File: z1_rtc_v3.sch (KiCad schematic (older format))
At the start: 61 parts, among them J1 Conn_01x05, J10 Conn_01x02, J2 61200621621, J3 Conn_01x11, J4 Conn_01x11, J5 Conn_01x11, J6 Conn_01x11, J7 691137710002, J8 USB_B_Micro, J9 Conn_01x02, U1 LCMXO2-1200HC-4SG32C, U2 ATmega328PB-AU, U3 FT230XS, Y1 Crystal_Small

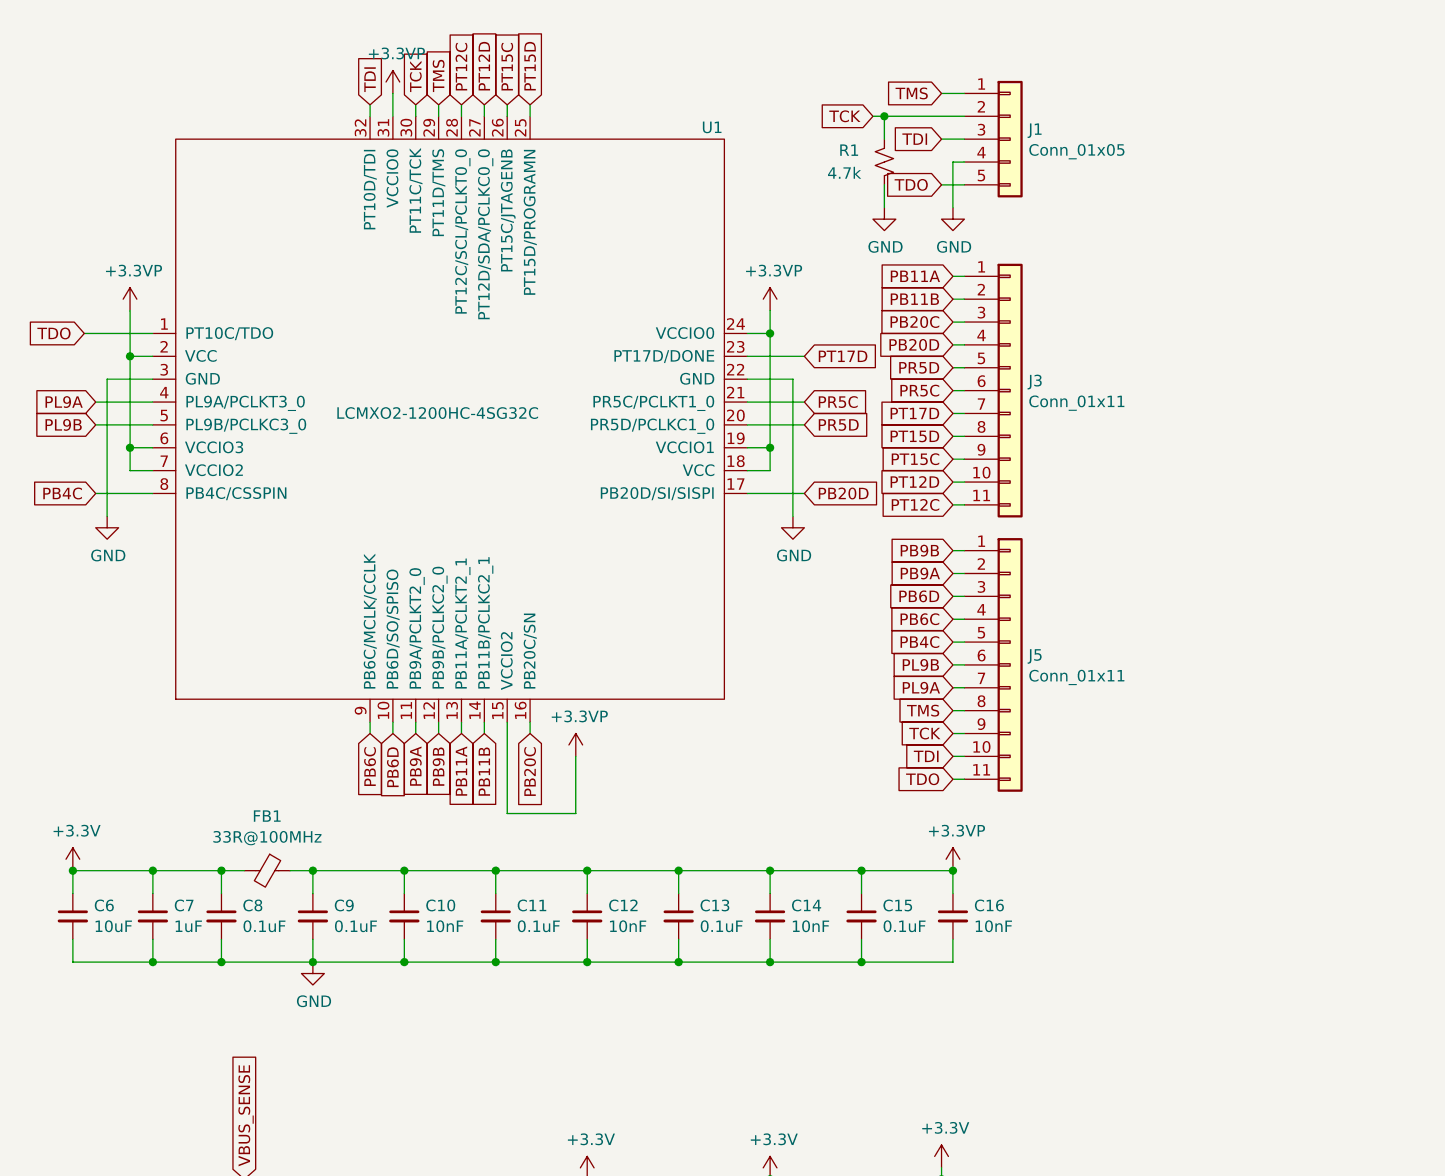
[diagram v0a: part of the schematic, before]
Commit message: board files for v3.2, with the tinyFPGA module
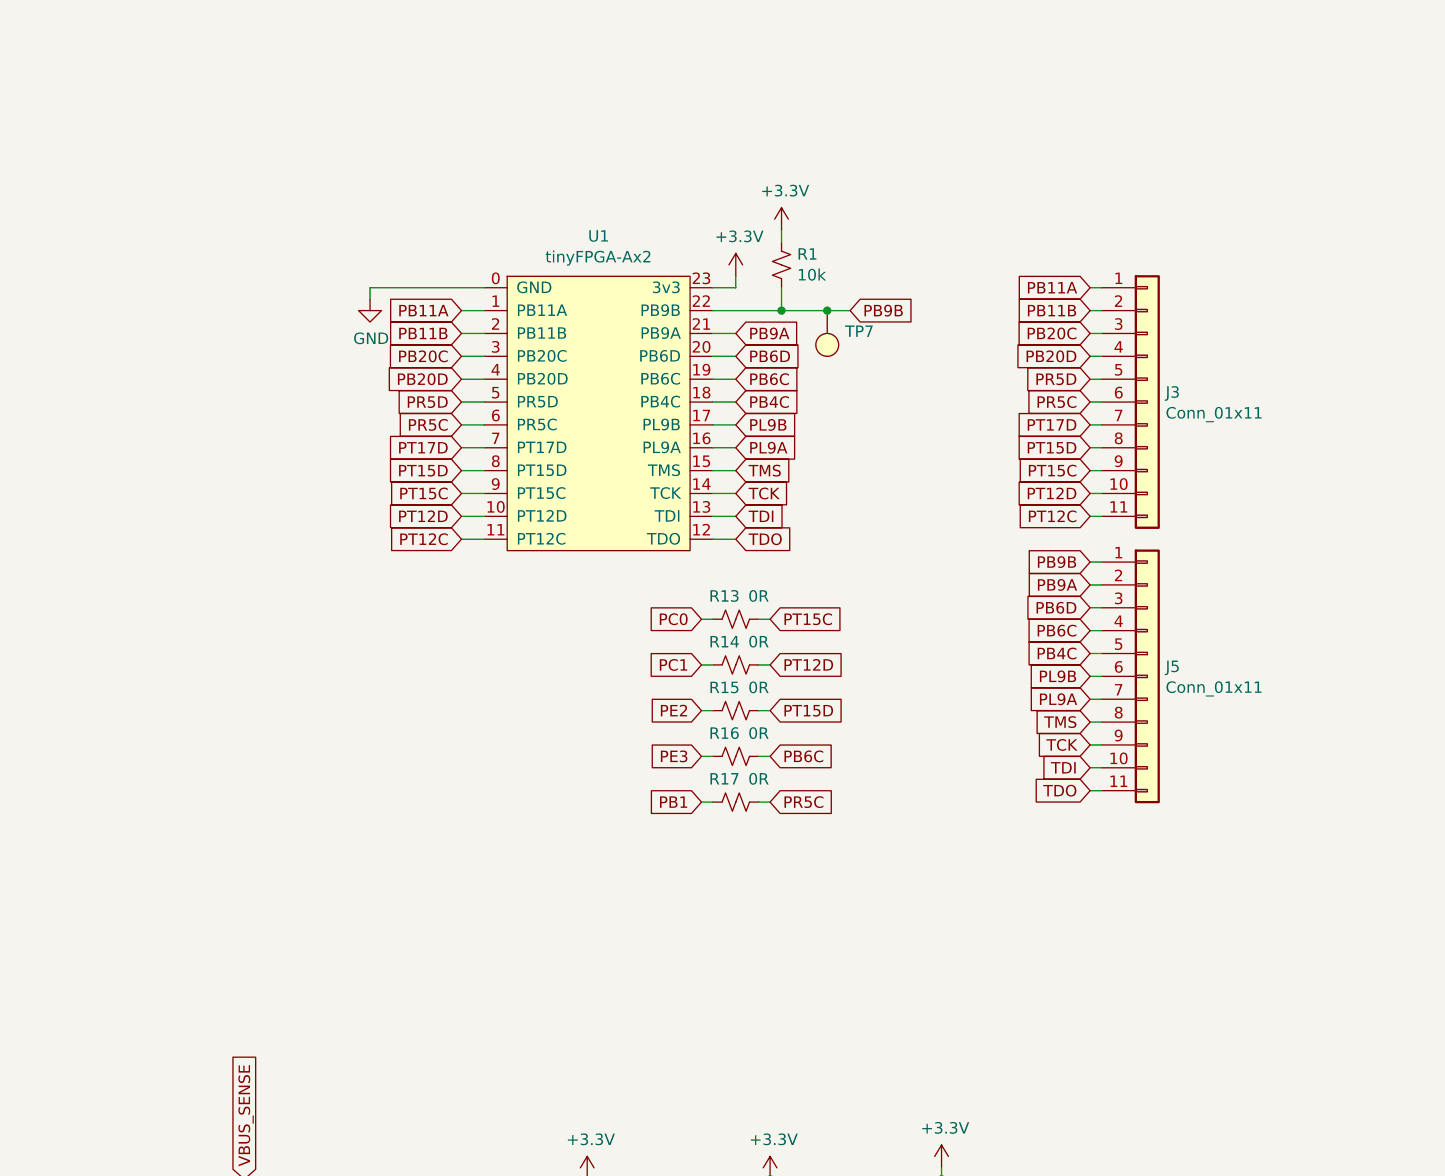
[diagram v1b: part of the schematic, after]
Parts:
- removed C10, C12, C14, C16: 10nF, Capacitor_SMD:C_0805_2012Metric, symbol Device:C_Small
- removed C11, C13, C15, C8, C9: 0.1uF, Capacitor_SMD:C_0603_1608Metric, symbol Device:C_Small
- removed C6: 10uF, Capacitor_SMD:C_0805_2012Metric, symbol Device:C_Small
- removed C7: 1uF, Capacitor_SMD:C_0603_1608Metric, symbol Device:C_Small
- removed FB1: 33R@100MHz, Capacitor_SMD:C_0603_1608Metric, symbol Device:Ferrite_Bead_Small
- removed J1: Conn_01x05, Connector_PinHeader_2.54mm:PinHeader_1x05_P2.54mm_Vertical, symbol Connector_Generic:Conn_01x05
- removed U1: LCMXO2-1200HC-4SG32C, Package_DFN_QFN:QFN-32-1EP_5x5mm_P0.5mm_EP3.1x3.1mm, symbol z1_rtc_v3:LCMXO2-1200HC-4SG32C
- added R13, R14, R15, R16, R17: 0R, Resistor_SMD:R_0603_1608Metric, symbol Device:R_Small_US
- added TP7: testpoint_smd_circ, z1_rtc_v3:test_point_smd_circ, symbol z1_rtc_v3:testpoint_smd_circ
- added U1: tinyFPGA-Ax2, z1_rtc_v3:tinyFPGA-Ax2, symbol z1_rtc_v3:tinyFPGA-Ax2
- R1: value 4.7k -> 10k; pn CRGH0603F4K7 -> RC0603JR-0710KL
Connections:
- net +3V3: now also R1.1, U1.23 (3v3)
- net GND: now also U1.0 (GND); no longer R1.2
- net PB1: now also R17.2
- net PB11A: now also U1.1 (PB11A)
- net PB11B: now also U1.2 (PB11B)
- net PB20C: now also U1.3 (PB20C)
- net PB20D: now also U1.4 (PB20D)
- net PB4C: now also U1.18 (PB4C)
- net PB6C: now also R16.1, U1.19 (PB6C)
- net PB6D: now also U1.20 (PB6D)
- net PB9A: now also U1.21 (PB9A)
- net PB9B: now also R1.2, TP7.~, U1.22 (PB9B)
- net PC0: now also R13.2
- net PC1: now also R14.2
- net PE2: now also R15.2
- net PE3: now also R16.2
- net PL9A: now also U1.16 (PL9A)
- net PL9B: now also U1.17 (PL9B)
- net PR5C: now also R17.1, U1.6 (PR5C)
- net PR5D: now also U1.5 (PR5D)
- net PT12C: now also U1.11 (PT12C)
- net PT12D: now also R14.1, U1.10 (PT12D)
- net PT15C: now also R13.1, U1.9 (PT15C)
- net PT15D: now also R15.1, U1.8 (PT15D)
- net PT17D: now also U1.7 (PT17D)
- net TCK: now also U1.14 (TCK); no longer R1.1
- net TDI: now also U1.13 (TDI)
- net TDO: now also U1.12 (TDO)
- net TMS: now also U1.15 (TMS)
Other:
- moved on the sheet: J3, J5
